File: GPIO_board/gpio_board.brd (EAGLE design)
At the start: 95.2 x 83.8 mm, 15 parts, among them J1 SWITCHES, J2 LED1, J3 LED2, Q1 IRF520, Q2 IRF520, Q3 IRF520, X1 PCI-E-164SLOT

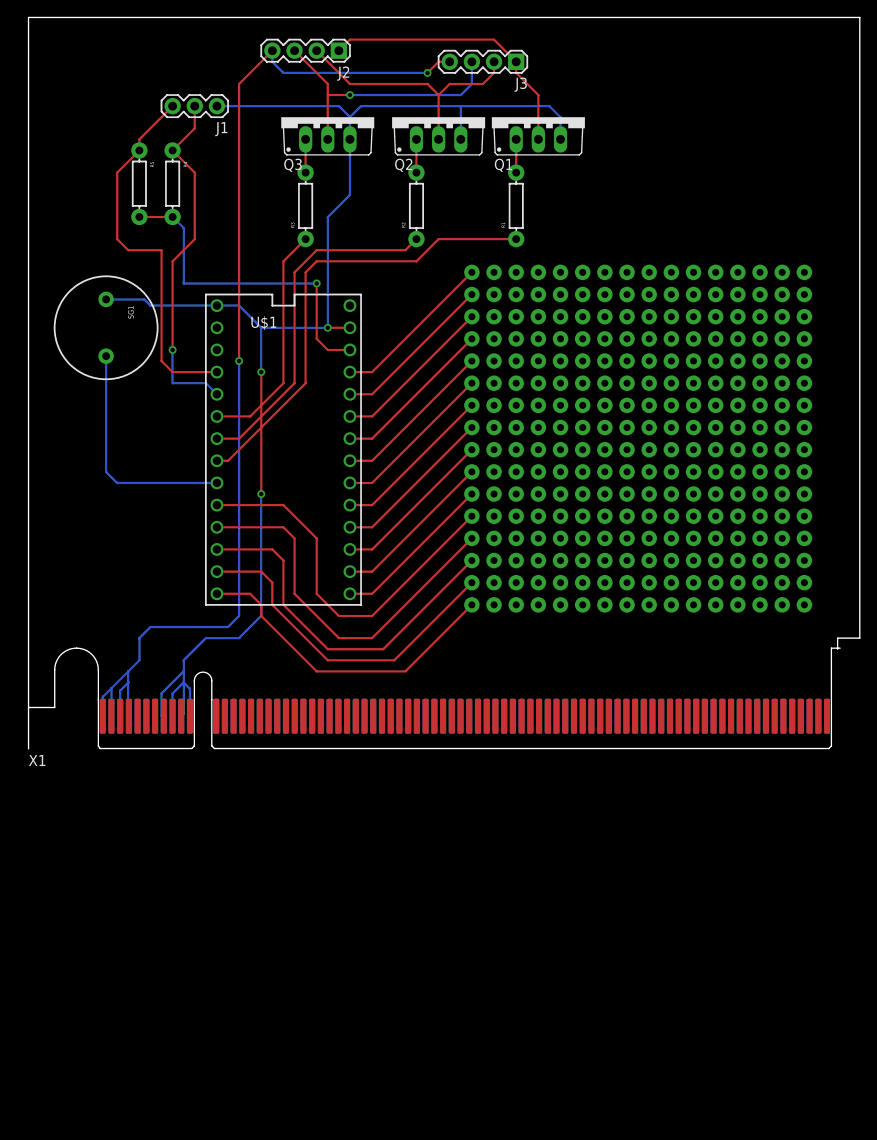
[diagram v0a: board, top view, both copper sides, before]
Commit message: fixed board outline and fixed some traces
figured out that the PCIe slot is in metric, so that requires metric
grid to get it aligned right.
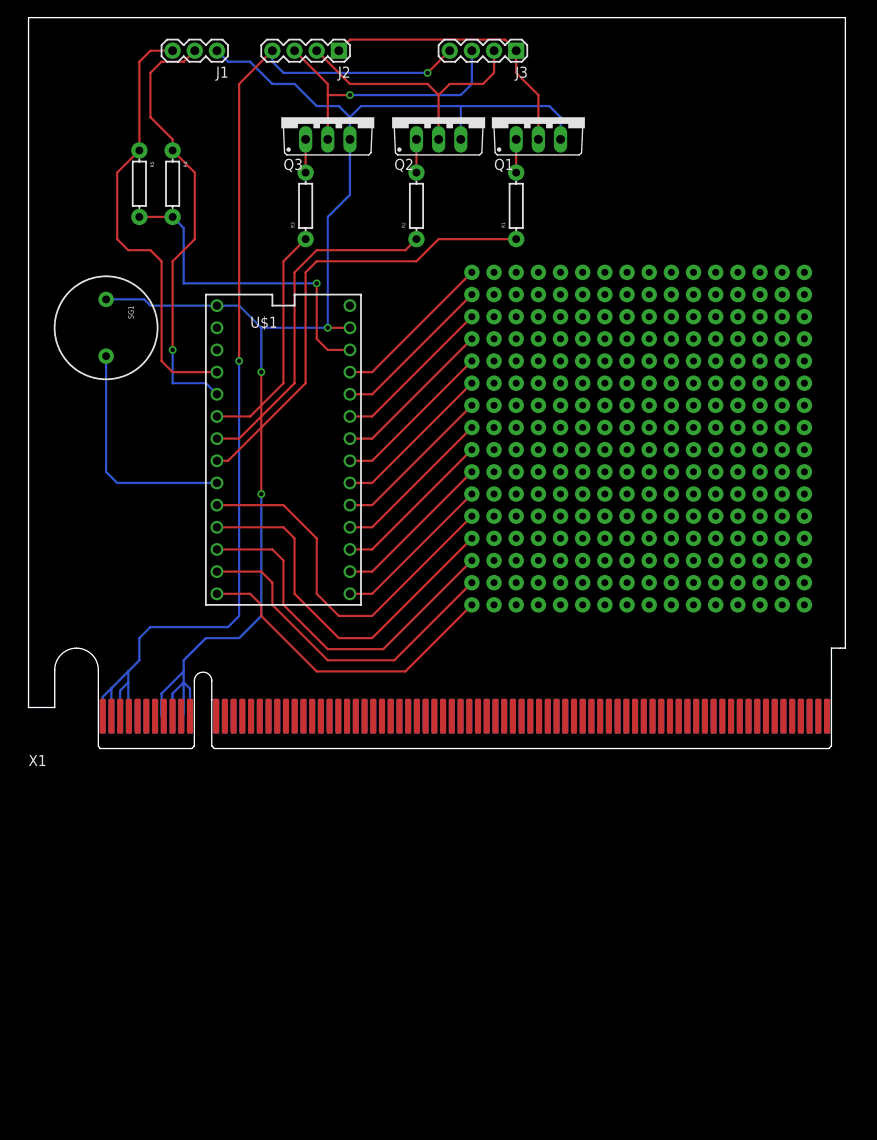
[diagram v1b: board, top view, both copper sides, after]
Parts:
- moved J1 6.35 mm to (21.6, 80.0)
- moved J3 1.27 mm to (55.9, 80.0)
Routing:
- net N$7: track 40.5 -> 50.5 mm
- net N$5: track 43.1 -> 50.1 mm
- net GND: track 167.3 -> 169.9 mm
- net N$6: track 29.8 -> 31.1 mm
- net N$10: track 31.3 -> 32.6 mm
- net N$4: track 31.8 -> 32.6 mm
- net VCC: track 124.9 -> 125.4 mm
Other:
- board size 95.2 x 83.8 mm -> 93.6 x 79 mm
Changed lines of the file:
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@@
 <board>
 <plain>
-<wire x1="0" y1="0" x2="0" y2="80" width="0" layer="20"/>
-<wire x1="0" y1="80.01" x2="0" y2="83.82" width="0" layer="20"/>
-<wire x1="0" y1="83.82" x2="95.25" y2="83.82" width="0" layer="20"/>
-<wire x1="95.25" y1="83.82" x2="95.25" y2="12.7" width="0" layer="20"/>
-<wire x1="95.25" y1="12.7" x2="92.71" y2="12.7" width="0" layer="20"/>
-<wire x1="92.71" y1="12.7" x2="92.71" y2="11.43" width="0" layer="20"/>
+<wire x1="0" y1="4.75" x2="0" y2="83.8" width="0" layer="20"/>
+<wire x1="0" y1="83.8" x2="93.6" y2="83.8" width="0" layer="20"/>
+<wire x1="93.6" y1="83.8" x2="93.6" y2="11.55" width="0" layer="20"/>
+<wire x1="93.6" y1="11.55" x2="93" y2="11.55" width="0" layer="20"/>
 </plain>
 <attributes>
@@
 </autorouter>
 <elements>
-<element name="J1" library="SparkFun-Connectors" package="1X03" value="SWITCHES" x="21.59" y="73.66" rot="R180"/>
+<element name="J1" library="SparkFun-Connectors" package="1X03" value="SWITCHES" x="21.59" y="80.01" rot="R180"/>
 <element name="J2" library="SparkFun-Connectors" package="1X04" value="LED1" x="35.56" y="80.01" rot="R180">
 <attribute name="PROD_ID" value="CONN-09696" x="35.56" y="80.01" size="1.778" layer="27" rot="R180" display="off"/>
 </element>
-<element name="J3" library="SparkFun-Connectors" package="1X04" value="LED2" x="55.88" y="78.74" rot="R180">
-<attribute name="PROD_ID" value="CONN-09696" x="55.88" y="78.74" size="1.778" layer="27" rot="R180" display="off"/>
+<element name="J3" library="SparkFun-Connectors" package="1X04" value="LED2" x="55.88" y="80.01" rot="R180">
+<attribute name="PROD_ID" value="CONN-09696" x="55.88" y="80.01" size="1.778" layer="27" rot="R180" display="off"/>
 </element>
 <element name="Q1" library="transistor-power" package="TO220BV" value="IRF520" x="58.42" y="72.39"/>
@@
 <wire x1="60.96" y1="72.39" x2="60.96" y2="69.85" width="0.254" layer="16"/>
 <wire x1="49.53" y1="69.85" x2="49.53" y2="73.66" width="0.254" layer="16"/>
-<wire x1="21.59" y1="73.66" x2="35.56" y2="73.66" width="0.254" layer="16"/>
 <wire x1="35.56" y1="73.66" x2="36.83" y2="72.39" width="0.254" layer="16"/>
 <wire x1="26.67" y1="48.26" x2="26.67" y2="43.18" width="0.254" layer="16"/>
@@
 <wire x1="13.26" y1="51.51" x2="13.97" y2="50.8" width="0.254" layer="16"/>
 <wire x1="13.97" y1="50.8" x2="21.59" y2="50.8" width="0.254" layer="16"/>
+<wire x1="35.56" y1="73.66" x2="33.02" y2="73.66" width="0.254" layer="16"/>
+<wire x1="33.02" y1="73.66" x2="30.48" y2="76.2" width="0.254" layer="16"/>
+<wire x1="30.48" y1="76.2" x2="27.94" y2="76.2" width="0.254" layer="16"/>
+<wire x1="27.94" y1="76.2" x2="25.4" y2="78.74" width="0.254" layer="16"/>
+<wire x1="25.4" y1="78.74" x2="22.86" y2="78.74" width="0.254" layer="16"/>
+<wire x1="22.86" y1="78.74" x2="21.59" y2="80.01" width="0.254" layer="16"/>
 </signal>
 <signal name="N$1">
@@
 <contactref element="Q1" pad="D"/>
 <contactref element="J3" pad="1"/>
-<wire x1="55.88" y1="78.74" x2="55.88" y2="77.47" width="0.254" layer="1"/>
+<wire x1="55.88" y1="80.01" x2="55.88" y2="77.47" width="0.254" layer="1"/>
 <wire x1="55.88" y1="77.47" x2="58.42" y2="74.93" width="0.254" layer="1"/>
 <wire x1="58.42" y1="74.93" x2="58.42" y2="69.85" width="0.254" layer="1"/>
 <wire x1="35.56" y1="80.01" x2="36.83" y2="81.28" width="0.254" layer="1"/>
-<wire x1="36.83" y1="81.28" x2="53.34" y2="81.28" width="0.254" layer="1"/>
-<wire x1="53.34" y1="81.28" x2="55.88" y2="78.74" width="0.254" layer="1"/>
+<wire x1="36.83" y1="81.28" x2="54.61" y2="81.28" width="0.254" layer="1"/>
+<wire x1="55.88" y1="80.01" x2="54.61" y2="81.28" width="0.254" layer="1"/>
 </signal>
 <signal name="N$6">
@@
 <wire x1="45.72" y1="76.2" x2="46.99" y2="74.93" width="0.254" layer="1"/>
 <wire x1="46.99" y1="74.93" x2="46.99" y2="69.85" width="0.254" layer="1"/>
-<wire x1="53.34" y1="78.74" x2="53.34" y2="77.47" width="0.254" layer="1"/>
+<wire x1="53.34" y1="80.01" x2="53.34" y2="77.47" width="0.254" layer="1"/>
 <wire x1="53.34" y1="77.47" x2="52.07" y2="76.2" width="0.254" layer="1"/>
 <wire x1="52.07" y1="76.2" x2="48.26" y2="76.2" width="0.254" layer="1"/>
@@
 <wire x1="34.29" y1="76.2" x2="34.29" y2="74.93" width="0.254" layer="1"/>
 <wire x1="34.29" y1="74.93" x2="34.29" y2="69.85" width="0.254" layer="1"/>
-<wire x1="50.8" y1="78.74" x2="50.8" y2="76.2" width="0.254" layer="16"/>
+<wire x1="50.8" y1="80.01" x2="50.8" y2="76.2" width="0.254" layer="16"/>
 <wire x1="50.8" y1="76.2" x2="49.53" y2="74.93" width="0.254" layer="16"/>
 <wire x1="49.53" y1="74.93" x2="36.83" y2="74.93" width="0.254" layer="16"/>
@@
 <wire x1="11.43" y1="7.62" x2="11.43" y2="3.82" width="0.254" layer="16"/>
 <wire x1="11.43" y1="3.82" x2="11.5" y2="3.75" width="0.254" layer="16"/>
-<wire x1="48.26" y1="78.74" x2="46.99" y2="78.74" width="0.254" layer="1"/>
-<wire x1="46.99" y1="78.74" x2="45.72" y2="77.47" width="0.254" layer="1"/>
+<wire x1="48.26" y1="80.01" x2="45.72" y2="77.47" width="0.254" layer="1"/>
 <via x="45.72" y="77.47" extent="1-16" drill="0.508"/>
 <wire x1="45.72" y1="77.47" x2="29.21" y2="77.47" width="0.254" layer="16"/>
@@
 <wire x1="21.59" y1="43.18" x2="16.51" y2="43.18" width="0.254" layer="1"/>
 <wire x1="16.51" y1="43.18" x2="15.24" y2="44.45" width="0.254" layer="1"/>
-<wire x1="15.24" y1="44.45" x2="15.24" y2="57.15" width="0.254" layer="1"/>
-<wire x1="15.24" y1="57.15" x2="11.43" y2="57.15" width="0.254" layer="1"/>
 <wire x1="11.43" y1="57.15" x2="10.16" y2="58.42" width="0.254" layer="1"/>
 <wire x1="10.16" y1="58.42" x2="10.16" y2="66.04" width="0.254" layer="1"/>
 <wire x1="10.16" y1="66.04" x2="12.7" y2="68.58" width="0.254" layer="1"/>
-<wire x1="12.7" y1="68.58" x2="12.7" y2="69.85" width="0.254" layer="1"/>
-<wire x1="12.7" y1="69.85" x2="16.51" y2="73.66" width="0.254" layer="1"/>
+<wire x1="12.7" y1="68.58" x2="12.7" y2="78.74" width="0.254" layer="1"/>
+<wire x1="12.7" y1="78.74" x2="13.97" y2="80.01" width="0.254" layer="1"/>
+<wire x1="13.97" y1="80.01" x2="16.51" y2="80.01" width="0.254" layer="1"/>
+<wire x1="15.24" y1="44.45" x2="15.24" y2="55.88" width="0.254" layer="1"/>
+<wire x1="15.24" y1="55.88" x2="13.97" y2="57.15" width="0.254" layer="1"/>
+<wire x1="13.97" y1="57.15" x2="11.43" y2="57.15" width="0.254" layer="1"/>
 </signal>
 <signal name="N$7">
@@
 <wire x1="16.51" y1="41.91" x2="20.32" y2="41.91" width="0.254" layer="16"/>
 <wire x1="20.32" y1="41.91" x2="21.59" y2="40.64" width="0.254" layer="16"/>
-<wire x1="16.51" y1="68.58" x2="19.05" y2="71.12" width="0.254" layer="1"/>
-<wire x1="19.05" y1="71.12" x2="19.05" y2="73.66" width="0.254" layer="1"/>
+<wire x1="16.51" y1="68.58" x2="16.51" y2="69.85" width="0.254" layer="1"/>
+<wire x1="16.51" y1="69.85" x2="13.97" y2="72.39" width="0.254" layer="1"/>
+<wire x1="13.97" y1="72.39" x2="13.97" y2="77.47" width="0.254" layer="1"/>
+<wire x1="13.97" y1="77.47" x2="15.24" y2="78.74" width="0.254" layer="1"/>
+<wire x1="15.24" y1="78.74" x2="17.78" y2="78.74" width="0.254" layer="1"/>
+<wire x1="17.78" y1="78.74" x2="19.05" y2="80.01" width="0.254" layer="1"/>
 </signal>
 <signal name="N$12">

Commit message: figured out ground planes
or did I? ???
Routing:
- net GND: track 169.9 -> 0.00 mm, vias 3 -> 0
- net VCC: track 125.4 -> 0.00 mm, vias 2 -> 0
- net N$11: track 52.3 -> 0.00 mm
- net N$7: track 50.5 -> 0.00 mm, vias 1 -> 0
- net N$5: track 50.1 -> 0.00 mm
- net N$25: track 42.9 -> 0.00 mm
- net N$13: track 42.9 -> 0.00 mm
- net N$26: track 41.1 -> 0.00 mm
- net N$9: track 39.8 -> 0.00 mm
- net N$27: track 38.6 -> 0.00 mm
- net 3.3V: track 37.9 -> 0.00 mm, vias 1 -> 0
- net N$28: track 36.8 -> 0.00 mm
- net N$4: track 32.6 -> 0.00 mm
- net N$10: track 32.6 -> 0.00 mm, vias 1 -> 0
- net N$6: track 31.1 -> 0.00 mm
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- added copper zone on layer 16, net GND

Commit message: routed some red traces.
GO RED TEAM
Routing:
- net N$13: track 0.00 -> 45.2 mm
- net N$25: track 0.00 -> 42.6 mm
- net N$26: track 0.00 -> 40.1 mm
- net N$27: track 0.00 -> 37.5 mm
- net N$28: track 0.00 -> 35.0 mm
- net N$24: track 0.00 -> 18.7 mm
- net N$23: track 0.00 -> 18.7 mm
- net N$22: track 0.00 -> 18.7 mm
- net N$21: track 0.00 -> 18.7 mm
- net N$18: track 0.00 -> 18.7 mm
- net N$17: track 0.00 -> 18.7 mm
- net N$16: track 0.00 -> 18.7 mm
- net N$15: track 0.00 -> 18.7 mm
- net N$14: track 0.00 -> 18.7 mm
- net N$20: track 0.00 -> 18.7 mm
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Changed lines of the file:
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@@
 <contactref element="U$1" pad="23/A9"/>
 <contactref element="U$2" pad="P$16"/>
-<wire x1="36.83" y1="43.18" x2="50.8" y2="54.61" width="0" layer="19" extent="1-1"/>
+<wire x1="36.83" y1="43.18" x2="39.37" y2="43.18" width="0.4064" layer="1"/>
+<wire x1="39.37" y1="43.18" x2="50.8" y2="54.61" width="0.4064" layer="1"/>
 </signal>
 <signal name="N$15">
 <contactref element="U$1" pad="22/A8"/>
 <contactref element="U$2" pad="P$15"/>
-<wire x1="36.83" y1="40.64" x2="50.8" y2="52.07" width="0" layer="19" extent="1-1"/>
+<wire x1="36.83" y1="40.64" x2="39.37" y2="40.64" width="0.4064" layer="1"/>
+<wire x1="39.37" y1="40.64" x2="50.8" y2="52.07" width="0.4064" layer="1"/>
 </signal>
 <signal name="N$16">
 <contactref element="U$1" pad="21/A7"/>
 <contactref element="U$2" pad="P$14"/>
-<wire x1="36.83" y1="38.1" x2="50.8" y2="49.53" width="0" layer="19" extent="1-1"/>
+<wire x1="36.83" y1="38.1" x2="39.37" y2="38.1" width="0.4064" layer="1"/>
+<wire x1="39.37" y1="38.1" x2="50.8" y2="49.53" width="0.4064" layer="1"/>
 </signal>
 <signal name="N$17">
 <contactref element="U$1" pad="20/A6"/>
 <contactref element="U$2" pad="P$13"/>
-<wire x1="36.83" y1="35.56" x2="50.8" y2="46.99" width="0" layer="19" extent="1-1"/>
+<wire x1="36.83" y1="35.56" x2="39.37" y2="35.56" width="0.4064" layer="1"/>
+<wire x1="39.37" y1="35.56" x2="50.8" y2="46.99" width="0.4064" layer="1"/>
 </signal>
 <signal name="N$18">
 <contactref element="U$1" pad="19/A5"/>
 <contactref element="U$2" pad="P$12"/>
-<wire x1="36.83" y1="33.02" x2="50.8" y2="44.45" width="0" layer="19" extent="1-1"/>
+<wire x1="36.83" y1="33.02" x2="39.37" y2="33.02" width="0.4064" layer="1"/>
+<wire x1="39.37" y1="33.02" x2="50.8" y2="44.45" width="0.4064" layer="1"/>
 </signal>
 <signal name="N$19">
 <contactref element="U$1" pad="18/A4"/>
 <contactref element="U$2" pad="P$11"/>
-<wire x1="36.83" y1="30.48" x2="50.8" y2="41.91" width="0" layer="19" extent="1-1"/>
+<wire x1="36.83" y1="30.48" x2="39.37" y2="30.48" width="0.4064" layer="1"/>
+<wire x1="39.37" y1="30.48" x2="50.8" y2="41.91" width="0.4064" layer="1"/>
 </signal>
 <signal name="N$20">
 <contactref element="U$1" pad="17/A3"/>
 <contactref element="U$2" pad="P$10"/>
-<wire x1="36.83" y1="27.94" x2="50.8" y2="39.37" width="0" layer="19" extent="1-1"/>
+<wire x1="36.83" y1="27.94" x2="39.37" y2="27.94" width="0.4064" layer="1"/>
+<wire x1="39.37" y1="27.94" x2="50.8" y2="39.37" width="0.4064" layer="1"/>
 </signal>
 <signal name="N$21">
 <contactref element="U$1" pad="16/A2"/>
 <contactref element="U$2" pad="P$9"/>
-<wire x1="36.83" y1="25.4" x2="50.8" y2="36.83" width="0" layer="19" extent="1-1"/>
+<wire x1="36.83" y1="25.4" x2="39.37" y2="25.4" width="0.4064" layer="1"/>
+<wire x1="39.37" y1="25.4" x2="50.8" y2="36.83" width="0.4064" layer="1"/>
 </signal>
 <signal name="N$22">
 <contactref element="U$1" pad="15/A1"/>
 <contactref element="U$2" pad="P$8"/>
-<wire x1="36.83" y1="22.86" x2="50.8" y2="34.29" width="0" layer="19" extent="1-1"/>
+<wire x1="36.83" y1="22.86" x2="39.37" y2="22.86" width="0.4064" layer="1"/>
+<wire x1="39.37" y1="22.86" x2="50.8" y2="34.29" width="0.4064" layer="1"/>
 </signal>
 <signal name="N$23">
 <contactref element="U$1" pad="14/A0"/>
 <contactref element="U$2" pad="P$7"/>
-<wire x1="36.83" y1="20.32" x2="50.8" y2="31.75" width="0" layer="19" extent="1-1"/>
+<wire x1="36.83" y1="20.32" x2="39.37" y2="20.32" width="0.4064" layer="1"/>
+<wire x1="39.37" y1="20.32" x2="50.8" y2="31.75" width="0.4064" layer="1"/>
 </signal>
 <signal name="N$24">
 <contactref element="U$1" pad="13"/>
 <contactref element="U$2" pad="P$6"/>
-<wire x1="36.83" y1="17.78" x2="50.8" y2="29.21" width="0" layer="19" extent="1-1"/>
+<wire x1="36.83" y1="17.78" x2="39.37" y2="17.78" width="0.4064" layer="1"/>
+<wire x1="39.37" y1="17.78" x2="50.8" y2="29.21" width="0.4064" layer="1"/>
 </signal>
 <signal name="N$13">
 <contactref element="U$1" pad="8"/>
 <contactref element="U$2" pad="P$5"/>
-<wire x1="21.59" y1="27.94" x2="50.8" y2="26.67" width="0" layer="19" extent="1-1"/>
+<wire x1="21.59" y1="27.94" x2="33.02" y2="27.94" width="0.4064" layer="1"/>
+<wire x1="33.02" y1="27.94" x2="34.29" y2="26.67" width="0.4064" layer="1"/>
+<wire x1="34.29" y1="26.67" x2="34.29" y2="16.51" width="0.4064" layer="1"/>
+<wire x1="34.29" y1="16.51" x2="35.56" y2="15.24" width="0.4064" layer="1"/>
+<wire x1="35.56" y1="15.24" x2="39.37" y2="15.24" width="0.4064" layer="1"/>
+<wire x1="39.37" y1="15.24" x2="50.8" y2="26.67" width="0.4064" layer="1"/>
 </signal>
 <signal name="N$25">
 <contactref element="U$1" pad="9"/>
 <contactref element="U$2" pad="P$4"/>
-<wire x1="21.59" y1="25.4" x2="50.8" y2="24.13" width="0" layer="19" extent="1-1"/>
+<wire x1="21.59" y1="25.4" x2="31.75" y2="25.4" width="0.4064" layer="1"/>
+<wire x1="31.75" y1="25.4" x2="33.02" y2="24.13" width="0.4064" layer="1"/>
+<wire x1="33.02" y1="24.13" x2="33.02" y2="16.51" width="0.4064" layer="1"/>
+<wire x1="33.02" y1="16.51" x2="35.56" y2="13.97" width="0.4064" layer="1"/>
+<wire x1="35.56" y1="13.97" x2="40.64" y2="13.97" width="0.4064" layer="1"/>
+<wire x1="40.64" y1="13.97" x2="50.8" y2="24.13" width="0.4064" layer="1"/>
 </signal>
 <signal name="N$26">
 <contactref element="U$1" pad="10"/>
 <contactref element="U$2" pad="P$3"/>
-<wire x1="21.59" y1="22.86" x2="50.8" y2="21.59" width="0" layer="19" extent="1-1"/>
+<wire x1="21.59" y1="22.86" x2="30.48" y2="22.86" width="0.4064" layer="1"/>
+<wire x1="30.48" y1="22.86" x2="31.75" y2="21.59" width="0.4064" layer="1"/>
+<wire x1="31.75" y1="21.59" x2="31.75" y2="16.51" width="0.4064" layer="1"/>
+<wire x1="31.75" y1="16.51" x2="35.56" y2="12.7" width="0.4064" layer="1"/>
+<wire x1="35.56" y1="12.7" x2="41.91" y2="12.7" width="0.4064" layer="1"/>
+<wire x1="41.91" y1="12.7" x2="50.8" y2="21.59" width="0.4064" layer="1"/>
 </signal>
 <signal name="N$27">
 <contactref element="U$1" pad="11"/>
 <contactref element="U$2" pad="P$2"/>
-<wire x1="21.59" y1="20.32" x2="50.8" y2="19.05" width="0" layer="19" extent="1-1"/>
+<wire x1="21.59" y1="20.32" x2="29.21" y2="20.32" width="0.4064" layer="1"/>
+<wire x1="29.21" y1="20.32" x2="30.48" y2="19.05" width="0.4064" layer="1"/>
+<wire x1="30.48" y1="19.05" x2="30.48" y2="16.51" width="0.4064" layer="1"/>
+<wire x1="30.48" y1="16.51" x2="35.56" y2="11.43" width="0.4064" layer="1"/>
+<wire x1="35.56" y1="11.43" x2="43.18" y2="11.43" width="0.4064" layer="1"/>
+<wire x1="43.18" y1="11.43" x2="50.8" y2="19.05" width="0.4064" layer="1"/>
 </signal>
 <signal name="N$28">
 <contactref element="U$1" pad="12"/>
 <contactref element="U$2" pad="P$1"/>
-<wire x1="21.59" y1="17.78" x2="50.8" y2="16.51" width="0" layer="19" extent="1-1"/>
+<wire x1="21.59" y1="17.78" x2="27.94" y2="17.78" width="0.4064" layer="1"/>
+<wire x1="27.94" y1="17.78" x2="35.56" y2="10.16" width="0.4064" layer="1"/>
+<wire x1="35.56" y1="10.16" x2="44.45" y2="10.16" width="0.4064" layer="1"/>
+<wire x1="44.45" y1="10.16" x2="50.8" y2="16.51" width="0.4064" layer="1"/>
 </signal>
 </signals>
